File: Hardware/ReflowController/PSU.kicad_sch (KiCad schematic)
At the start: 2 parts, among them U1 TSR_1-2450, U2 LD1117S33TR_SOT223

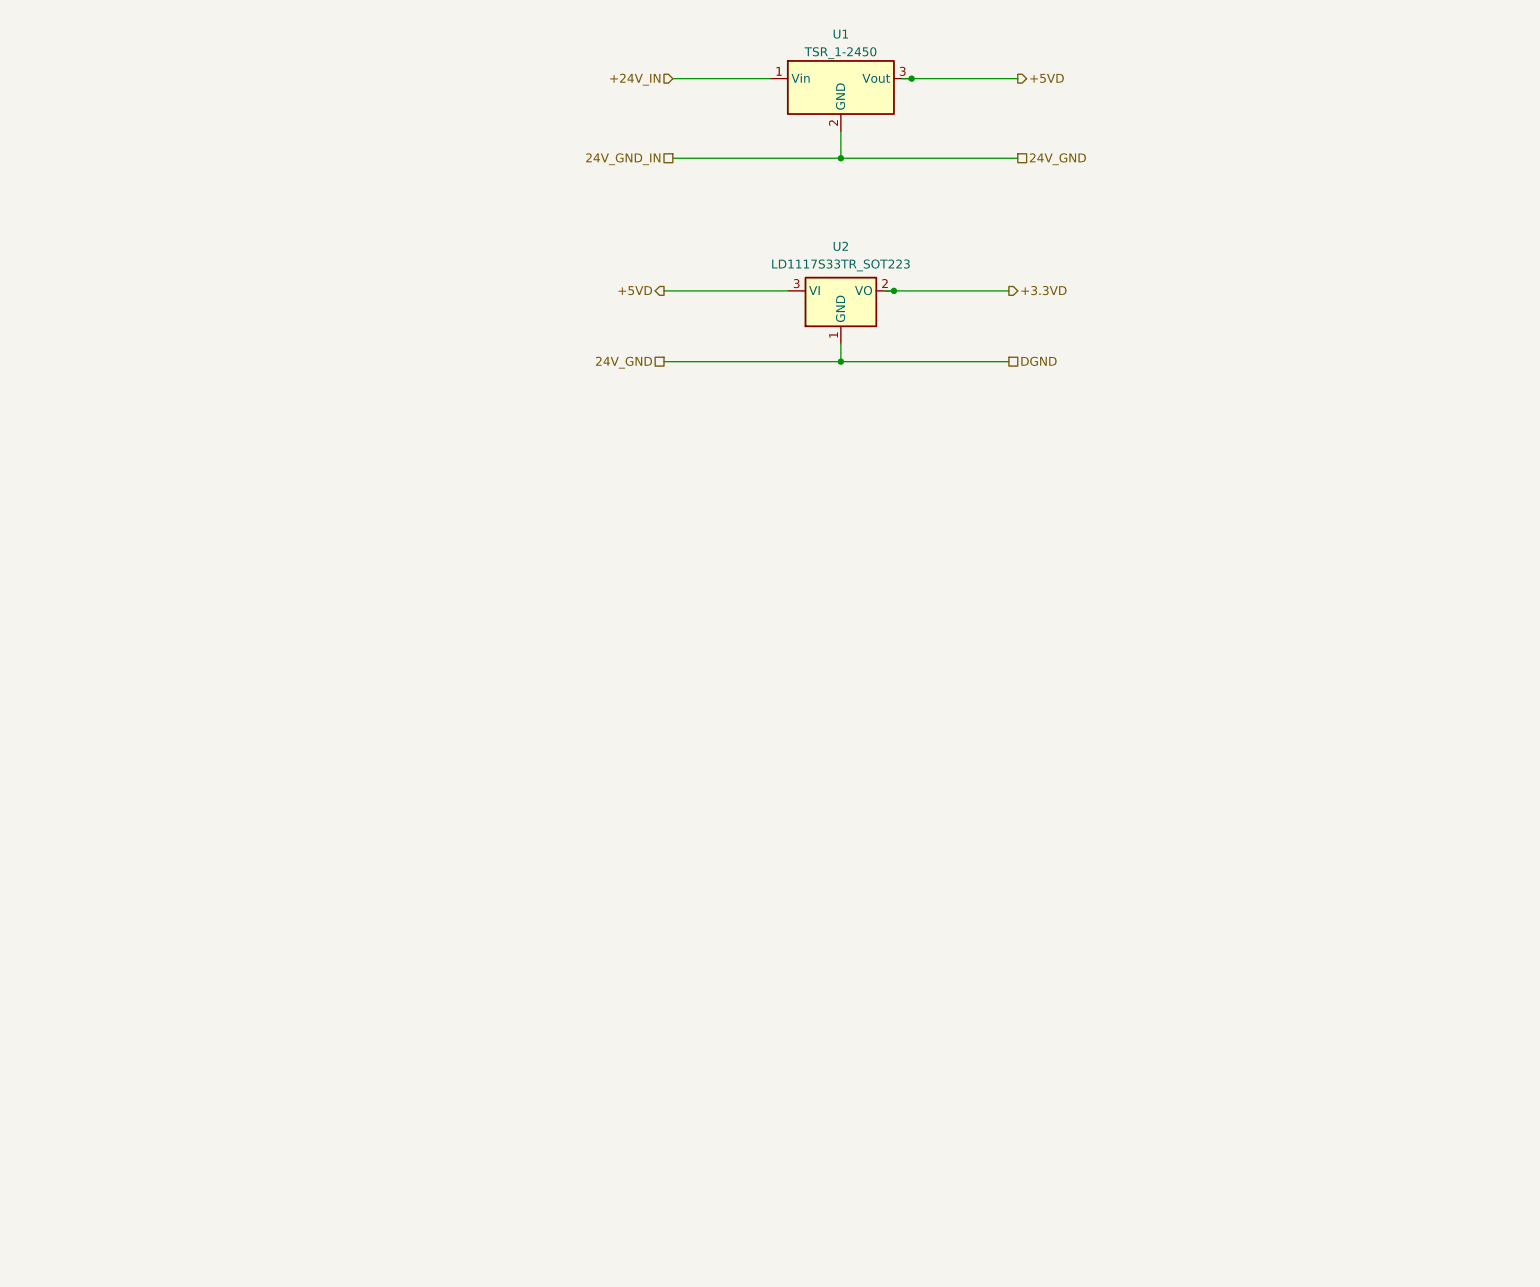
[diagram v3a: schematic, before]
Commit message: added the schematic of the updated pwerAndUi branch(with uC schematic update
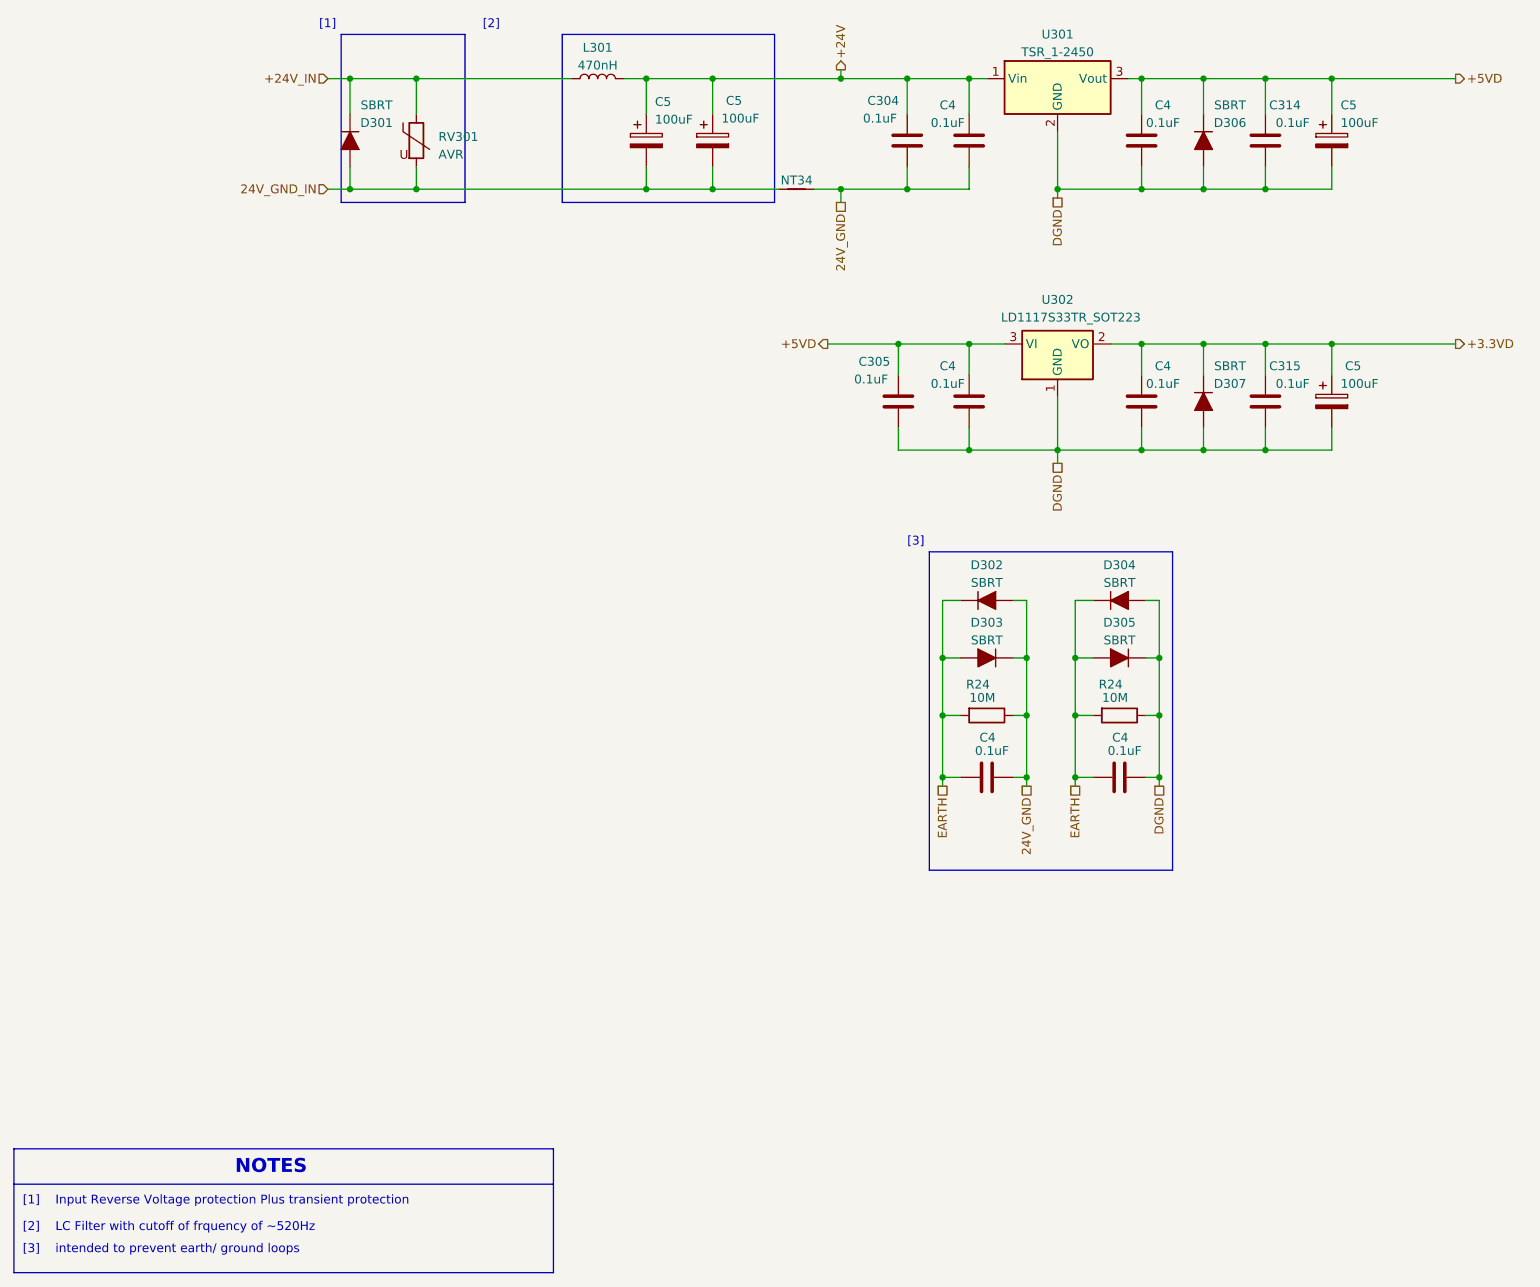
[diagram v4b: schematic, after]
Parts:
- added C304, C305, C314, C315: 0.1uF, Capacitor_THT:C_Rect_L7.2mm_W2.5mm_P5.00mm_FKS2_FKP2_MKS2_MKP2, symbol Ampli50W-rescue:C
- added C4 (x6): 0.1uF, Capacitor_SMD:C_1206_3216Metric, symbol Device:C
- added C5 (x4): 100uF, Capacitor_SMD:CP_Elec_8x10.5, symbol Device:C_Polarized
- added D301, D302, D303, D304, D305, D306, D307: SBRT, Diode_SMD:D_SMA_Handsoldering, symbol Ampli50W-rescue:D_ALT
- added L301: 470nH, 020_SMD_Inductors:2520, symbol Device:L
- added NT34: NetTie_2, NetTie:NetTie-2_SMD_Pad2.0mm, symbol Device:NetTie_2
- added R24 (x2): 10M, Resistor_SMD:R_1206_3216Metric, symbol Device:R
- added RV301: AVR, Resistor_SMD:R_0603_1608Metric_Pad0.98x0.95mm_HandSolder, symbol Device:Varistor
- renumbered U1 to U301, U2 to U302
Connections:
- net +24V_IN: now also D301.1 (K), L301.1, RV301.1; no longer U301.1 (Vin)
- net +3.3VD: now also C315.1, C4.2, C5.1, D307.1 (K)
- net +5VD: now also C305.1, C314.1, C4.2, C4.2, C5.1, D306.1 (K)
- net 24V_GND: now also C304.2, C4.1, C4.2, D302.2 (A), D303.1 (K), NT34.2, R24.1; no longer U301.2 (GND), U302.1 (GND)
- new net +24V: C304.1, C4.2, C5.1, C5.1, L301.2, U301.1 (Vin)
- new net 24V_GND_IN: C5.2, C5.2, D301.2 (A), NT34.1, RV301.2
- new net DGND: C305.2, C314.2, C315.2, C4.1, C4.1, C4.1, C4.2, C5.2, C5.2, D304.2 (A), D305.1 (K), D306.2 (A), D307.2 (A), R24.1, U301.2 (GND), U302.1 (GND)
- new net EARTH: C4.1, C4.1, D302.1 (K), D303.2 (A), D304.1 (K), D305.2 (A), R24.2, R24.2
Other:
- note added: "NOTES"
- note added: "[1]"
- note added: "[1] Input Reverse Voltage protection Plus transient protection"
- note added: "[2]"
- note added: "[2] LC Filter with cutoff of frquency of ~520Hz"
- note added: "[3]"
- note added: "[3] intended to prevent earth/ ground loops"
- moved on the sheet: U301, U302

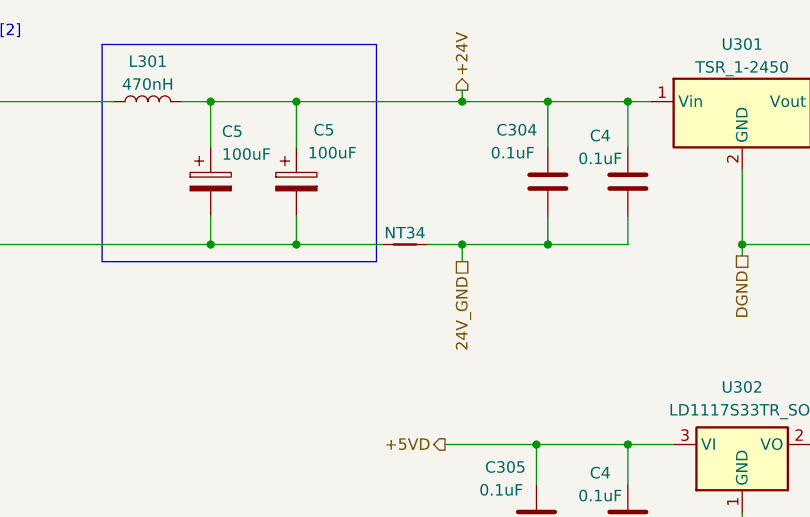
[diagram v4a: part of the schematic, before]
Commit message: Finished rewiev with Edwin, Need TO connect he HSS and DO the labeling
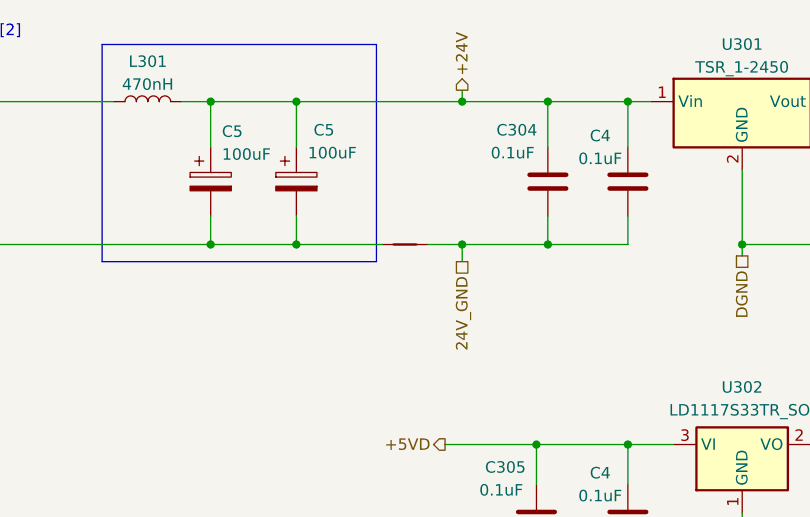
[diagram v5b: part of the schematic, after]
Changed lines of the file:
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@@
     (in_bom yes) (on_board yes) (dnp no)
     (property "Reference" "NT34" (at 125.73 40.005 0)
-      (effects (font (size 1.27 1.27)))
+      (effects (font (size 1.27 1.27)) hide)
     )
     (property "Value" "NetTie_2" (at 125.73 39.37 0)

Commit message: work on BOM cleanup
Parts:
- C304, C305, C314, C315: disti_mo 495-5055-1-ND -> (none); disti_no (none) -> 495-5055-1-ND
- D301, D302, D303, D304, D305, D306, D307: disit digikey -> (none); disti (none) -> digikey
- RV301: disit_no 445-2543-2-ND -> (none); disti_no (none) -> 445-2543-2-ND
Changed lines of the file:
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@@
       (effects (font (size 1.27 1.27)) hide)
     )
-    (property "disit" "digikey" (at 172.085 108.585 90)
+    (property "disit" "" (at 172.085 108.585 90)
       (effects (font (size 1.27 1.27)) hide)
     )
     (property "disti_no" "SBRT5A50SA-13DICT-ND" (at 172.085 108.585 90)
+      (effects (font (size 1.27 1.27)) hide)
+    )
+    (property "disti" "digikey" (at 172.085 108.585 0)
       (effects (font (size 1.27 1.27)) hide)
     )
@@
       (effects (font (size 1.27 1.27)) hide)
     )
-    (property "disit" "digikey" (at 153.035 100.33 90)
+    (property "disit" "" (at 153.035 100.33 90)
       (effects (font (size 1.27 1.27)) hide)
     )
     (property "disti_no" "SBRT5A50SA-13DICT-ND" (at 153.035 100.33 90)
+      (effects (font (size 1.27 1.27)) hide)
+    )
+    (property "disti" "digikey" (at 153.035 100.33 0)
       (effects (font (size 1.27 1.27)) hide)
     )
@@
       (effects (font (size 1.27 1.27)) hide)
     )
-    (property "disti_mo" "495-5055-1-ND" (at 141.605 34.29 0)
+    (property "disti_mo" "" (at 141.605 34.29 0)
+      (effects (font (size 1.27 1.27)) hide)
+    )
+    (property "disti_no" "495-5055-1-ND" (at 141.605 34.29 0)
       (effects (font (size 1.27 1.27)) hide)
     )
@@
       (effects (font (size 1.27 1.27)) hide)
     )
-    (property "disit" "digikey" (at 153.035 108.585 90)
+    (property "disit" "" (at 153.035 108.585 90)
       (effects (font (size 1.27 1.27)) hide)
     )
     (property "disti_no" "SBRT5A50SA-13DICT-ND" (at 153.035 108.585 90)
+      (effects (font (size 1.27 1.27)) hide)
+    )
+    (property "disti" "digikey" (at 153.035 108.585 0)
       (effects (font (size 1.27 1.27)) hide)
     )
@@
       (effects (font (size 1.27 1.27)) hide)
     )
-    (property "disit_no" "445-2543-2-ND" (at 71.12 34.29 0)
+    (property "disit_no" "" (at 71.12 34.29 0)
+      (effects (font (size 1.27 1.27)) hide)
+    )
+    (property "disti_no" "445-2543-2-ND" (at 71.12 34.29 0)
       (effects (font (size 1.27 1.27)) hide)
     )
@@
       (effects (font (size 1.27 1.27)) hide)
     )
-    (property "disti_mo" "495-5055-1-ND" (at 140.335 71.755 0)
+    (property "disti_mo" "" (at 140.335 71.755 0)
+      (effects (font (size 1.27 1.27)) hide)
+    )
+    (property "disti_no" "495-5055-1-ND" (at 140.335 71.755 0)
       (effects (font (size 1.27 1.27)) hide)
     )
@@
       (effects (font (size 1.27 1.27)) hide)
     )
-    (property "disit" "digikey" (at 61.595 34.29 90)
+    (property "disit" "" (at 61.595 34.29 90)
       (effects (font (size 1.27 1.27)) hide)
     )
     (property "disti_no" "SBRT5A50SA-13DICT-ND" (at 61.595 34.29 90)
+      (effects (font (size 1.27 1.27)) hide)
+    )
+    (property "disti" "digikey" (at 61.595 34.29 0)
       (effects (font (size 1.27 1.27)) hide)
     )
@@
       (effects (font (size 1.27 1.27)) hide)
     )
-    (property "disit" "digikey" (at 172.085 100.33 90)
+    (property "disit" "" (at 172.085 100.33 90)
       (effects (font (size 1.27 1.27)) hide)
     )
     (property "disti_no" "SBRT5A50SA-13DICT-ND" (at 172.085 100.33 90)
+      (effects (font (size 1.27 1.27)) hide)
+    )
+    (property "disti" "digikey" (at 172.085 100.33 0)
       (effects (font (size 1.27 1.27)) hide)
     )
@@
       (effects (font (size 1.27 1.27)) hide)
     )
-    (property "disti_mo" "495-5055-1-ND" (at 193.04 34.29 0)
+    (property "disti_mo" "" (at 193.04 34.29 0)
+      (effects (font (size 1.27 1.27)) hide)
+    )
+    (property "disti_no" "495-5055-1-ND" (at 193.04 34.29 0)
       (effects (font (size 1.27 1.27)) hide)
     )
@@
       (effects (font (size 1.27 1.27)) hide)
     )
-    (property "disit" "digikey" (at 184.15 71.755 90)
+    (property "disit" "" (at 184.15 71.755 90)
       (effects (font (size 1.27 1.27)) hide)
     )
     (property "disti_no" "SBRT5A50SA-13DICT-ND" (at 184.15 71.755 90)
+      (effects (font (size 1.27 1.27)) hide)
+    )
+    (property "disti" "digikey" (at 184.15 71.755 0)
       (effects (font (size 1.27 1.27)) hide)
     )
@@
       (effects (font (size 1.27 1.27)) hide)
     )
-    (property "disti_mo" "495-5055-1-ND" (at 193.04 71.755 0)
+    (property "disti_mo" "" (at 193.04 71.755 0)
+      (effects (font (size 1.27 1.27)) hide)
+    )
+    (property "disti_no" "495-5055-1-ND" (at 193.04 71.755 0)
       (effects (font (size 1.27 1.27)) hide)
     )
@@
       (effects (font (size 1.27 1.27)) hide)
     )
-    (property "disit" "digikey" (at 184.15 34.29 90)
+    (property "disit" "" (at 184.15 34.29 90)
       (effects (font (size 1.27 1.27)) hide)
     )
@@
       (effects (font (size 1.27 1.27)) hide)
     )
+    (property "disti" "digikey" (at 184.15 34.29 0)
+      (effects (font (size 1.27 1.27)) hide)
+    )
